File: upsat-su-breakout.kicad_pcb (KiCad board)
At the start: 2 copper layers, 36 x 26 mm, 9 parts, among them P1 SU, P2 EPS, P3 OBC, P4 RBF, P5 STM_0, P6 STM_1, P7 STM_2, P8 STM_3, P9 STM_4

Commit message: Rerouting GND.
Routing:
- net /STM_SHIELD: track 56.1 -> 68.9 mm, vias 0 -> 1
- net /GND: track 99.7 -> 110.2 mm, vias 7 -> 9
- net /STM_TH_RET_3: track 14.2 -> 16.7 mm

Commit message: Update layout for better fitting.
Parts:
- added G***: LOGO, w_logo:Logo_silk_OSHW_6x6mm, F.Cu at (195.2, 110.5)
- P2, P3: footprint hrs-df11:hrs-df11-6dp-2dsa -> hrs-df11:hrs-df11-6dp-2ds; moved to B.Cu
- P4, P5: footprint hrs-df11:hrs-df11-4dp-2dsa -> hrs-df11:hrs-df11-4dp-2ds; moved to B.Cu
- P6, P7, P8, P9: moved to B.Cu
- moved P8 29.1 mm to (189.5, 106.2), turned to 90 degrees
- moved P9 28.6 mm to (183.2, 105.2), turned to 0 degrees
- moved P6 27.3 mm to (175.0, 105.2), turned to 0 degrees
- moved P2 27.2 mm to (189.5, 97.8), turned to 90 degrees
- moved P7 24.9 mm to (166.8, 105.2), turned to 0 degrees
- moved P1 19.9 mm to (170.8, 98.0)
- moved P4 13.8 mm to (152.0, 106.5), turned to 270 degrees
- moved P3 6.91 mm to (152.0, 98.0), turned to 270 degrees
- moved P5 4.65 mm to (158.5, 105.2), turned to 0 degrees
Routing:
- net (no net): track 0.00 -> 55.0 mm
- net /STM_TH_RET_2: track 43.6 -> 12.0 mm, vias 0 -> 1
- net /GND: track 110.2 -> 134.4 mm, vias 9 -> 12
- net /STM_TH_RET_0: track 5.54 -> 28.9 mm
- net /STM_SHIELD: track 68.9 -> 51.4 mm, vias 1 -> 0
- net /STM_TH_GO_0: track 13.2 -> 29.0 mm, vias 1 -> 0
- net /STM_TH_GO_2: track 31.0 -> 16.0 mm, vias 0 -> 2
- net /MNLP_TH_RET: track 9.96 -> 21.9 mm
- net /MNLP_RX: track 9.89 -> 20.2 mm, vias 1 -> 0
- net /STM_TH_RET_1: track 12.2 -> 4.50 mm
- net /STM_TH_GO_1: track 16.5 -> 8.85 mm
- net /BIAS_DISARM_GND: track 14.3 -> 19.4 mm
- net /MNLP_TX: track 9.93 -> 14.9 mm
- net /+5: track 10.9 -> 15.7 mm
- net /STM_TH_RET_3: track 16.7 -> 21.5 mm
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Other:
- board size 36 x 26 mm -> 56 x 21 mm
- board text added: "UPSat SU Breakout"

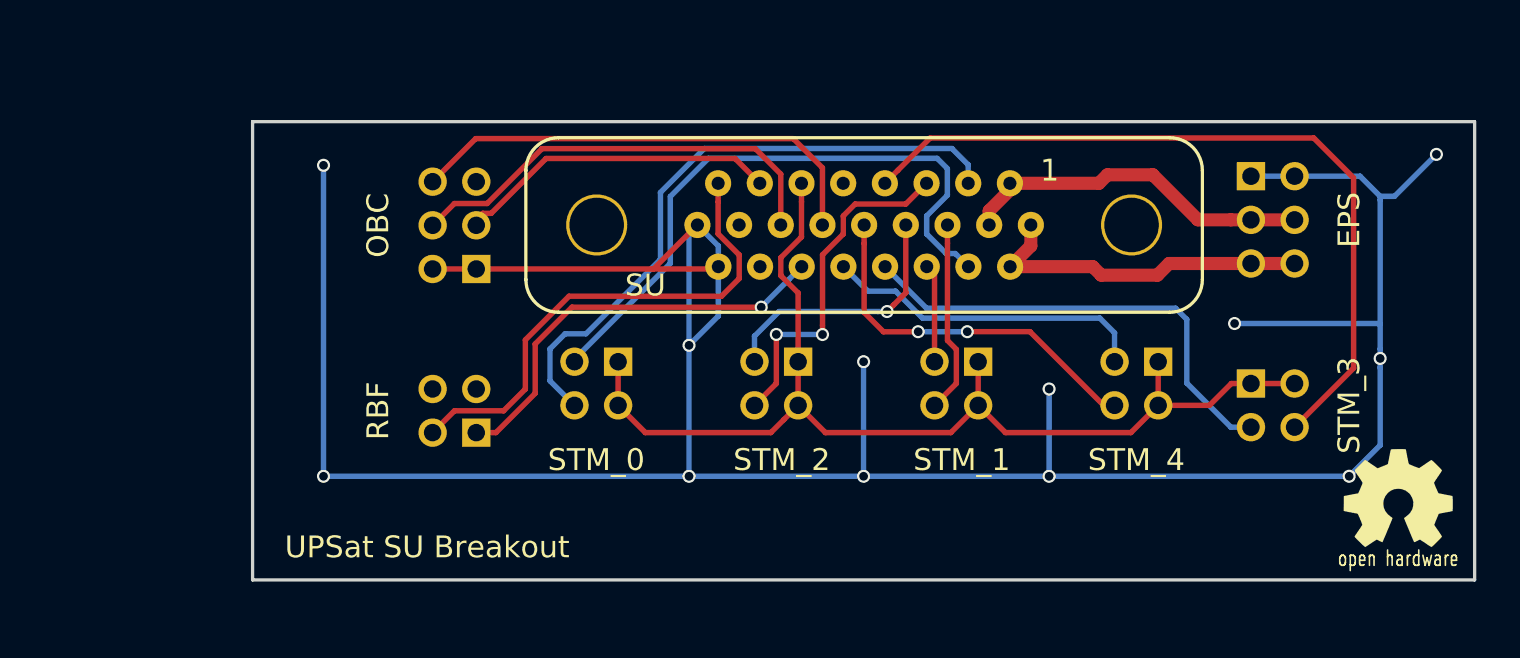
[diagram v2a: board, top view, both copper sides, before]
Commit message: Rerouting some connections.
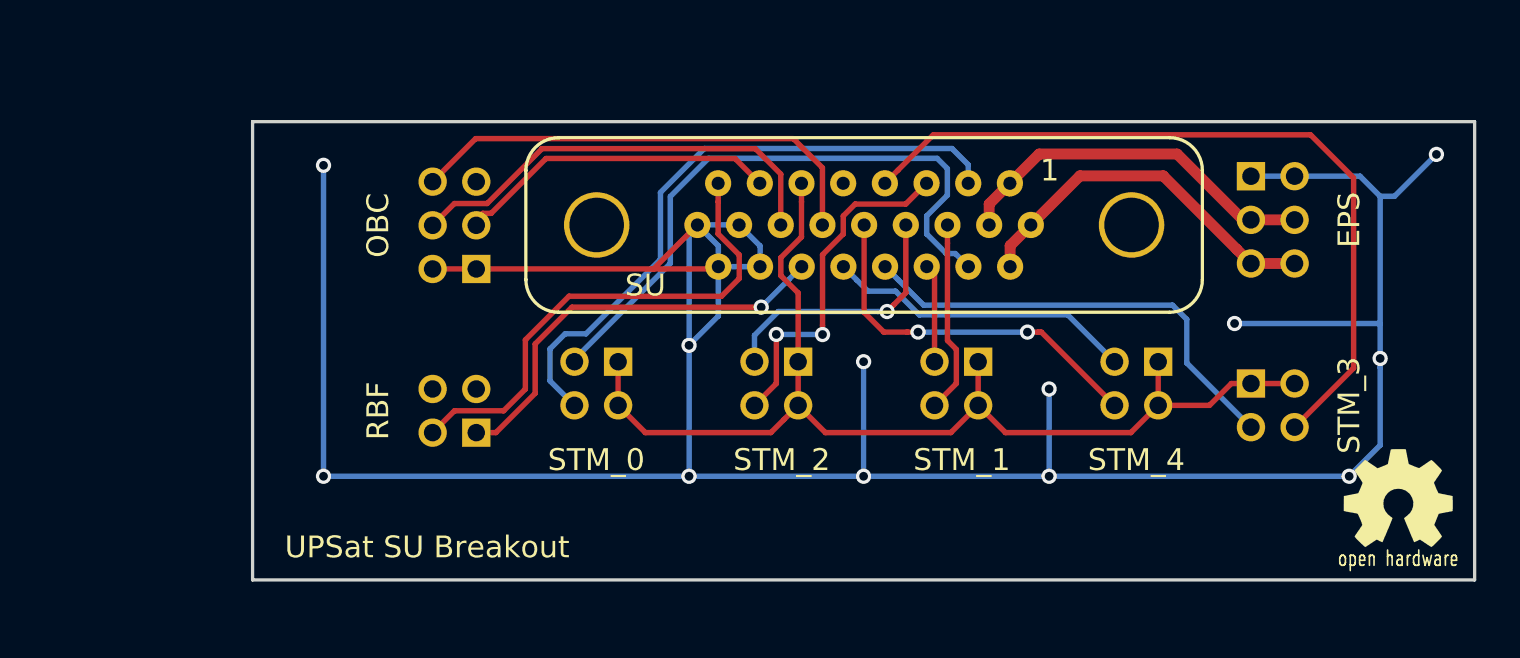
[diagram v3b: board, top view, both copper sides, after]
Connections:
- P1 pad 23: (no net) -> /GND
- P1 pad 24: (no net) -> /GND
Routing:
- net /GND: track 134.4 -> 140.5 mm
- net /+5: track 15.7 -> 17.0 mm
- net /+3V3: track 16.4 -> 17.5 mm
- net /STM_TH_RET_4: track 15.0 -> 14.2 mm
- net /STM_TH_RET_3: track 21.5 -> 21.0 mm
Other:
- net class Default: via_dia 0.6 -> 0.7
- net class PWR: clearance 0.6 -> 0.5; trace_width 0.6 -> 0.5; via_drill 0.4 -> 0.5
